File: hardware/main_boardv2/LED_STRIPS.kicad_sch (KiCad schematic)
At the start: 8 parts, among them IC801 SN74LV1T34DBVR, J801 Conn_01x03_Pin

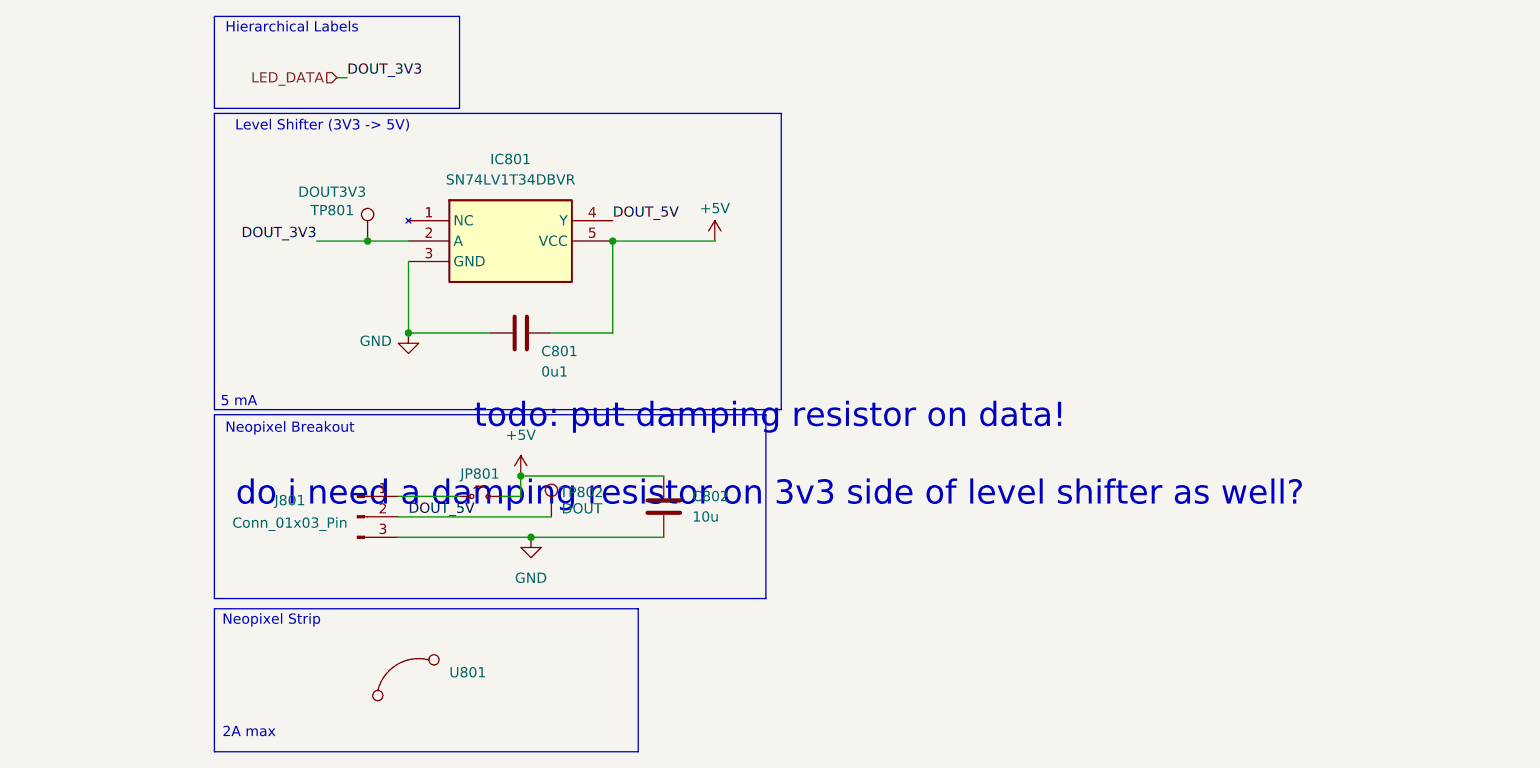
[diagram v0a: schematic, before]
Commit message: dubious hardware schematic 'done'. need to go back and revise passives and verify IC connections, esp the DAC. modified readme
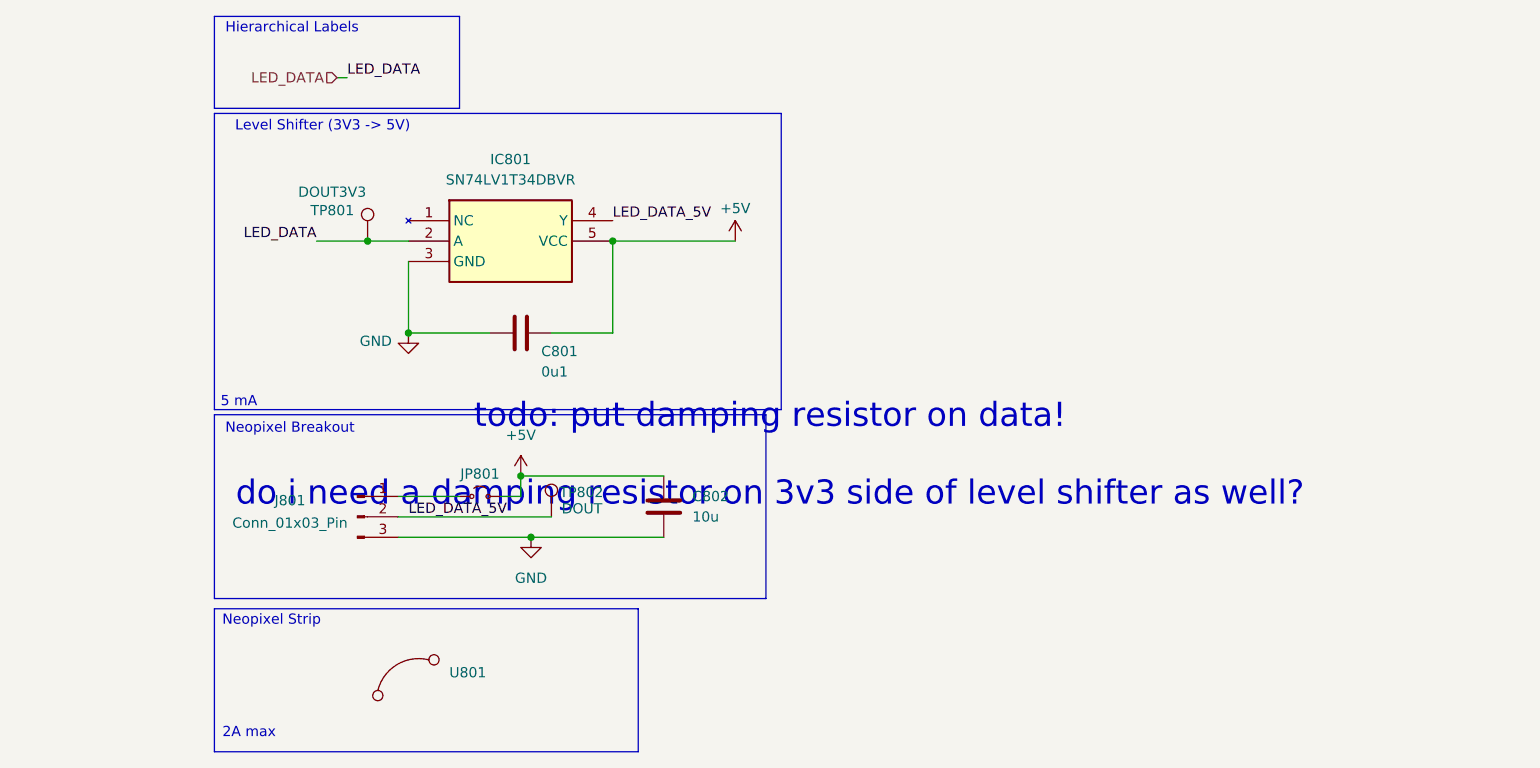
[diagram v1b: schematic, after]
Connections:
- net DOUT_5V renamed LED_DATA_5V
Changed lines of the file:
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@@
 	(wire
 		(pts
-			(xy 63.5 41.91) (xy 76.2 41.91)
+			(xy 63.5 41.91) (xy 78.74 41.91)
 		)
 		(stroke
@@
 		)
 	)
-	(label "DOUT_3V3"
+	(label "LED_DATA_5V"
+		(at 38.1 76.2 0)
+		(effects
+			(font
+				(size 1.27 1.27)
+			)
+			(justify left bottom)
+		)
+	)
+	(label "LED_DATA"
 		(at 30.48 21.59 0)
 		(effects
@@
 		)
 	)
-	(label "DOUT_3V3"
+	(label "LED_DATA"
 		(at 26.67 41.91 180)
 		(effects
@@
 		)
 	)
-	(label "DOUT_5V"
-		(at 38.1 76.2 0)
-		(effects
-			(font
-				(size 1.27 1.27)
-			)
-			(justify left bottom)
-		)
-	)
-	(label "DOUT_5V"
+	(label "LED_DATA_5V"
 		(at 63.5 39.37 0)
 		(effects
@@
 	(symbol
 		(lib_id "power:+5V")
-		(at 76.2 41.91 0)
+		(at 78.74 41.91 0)
 		(unit 1)
 		(exclude_from_sim no)
@@
 		(dnp no)
 		(property "Reference" "#PWR0804"
-			(at 76.2 45.72 0)
+			(at 78.74 45.72 0)
 			(effects
 				(font
@@
 		)
 		(property "Value" "+5V"
-			(at 76.2 37.846 0)
+			(at 78.74 37.846 0)
 			(effects
 				(font
@@
 		)
 		(property "Footprint" ""
-			(at 76.2 41.91 0)
+			(at 78.74 41.91 0)
 			(effects
 				(font
@@
 		)
 		(property "Datasheet" ""
-			(at 76.2 41.91 0)
+			(at 78.74 41.91 0)
 			(effects
 				(font
@@
 		)
 		(property "Description" "Power symbol creates a global label with name \"+5V\""
-			(at 76.2 41.91 0)
-			(effects
-				(font
+			(at 78.74 41.91 0)
+			(effects
+				(font

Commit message: schematic sorta done? resized all RC packages to 0805
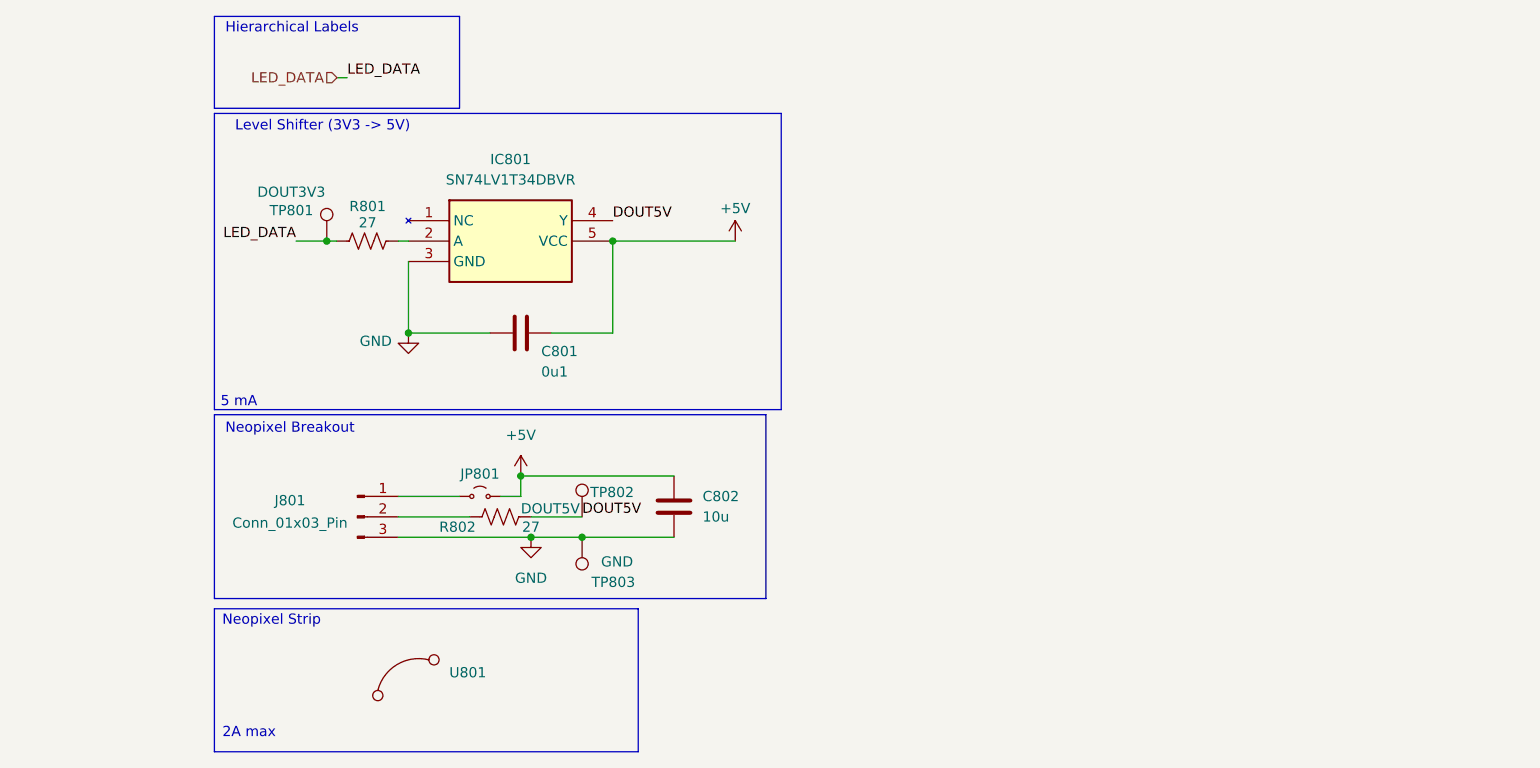
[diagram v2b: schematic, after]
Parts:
- added R801, R802: 27, Resistor_SMD:R_0805_2012Metric, symbol Device:R_US
- added TP803: GND, SamacSys_Parts:bettertestpoint2, symbol Connector:TestPoint
- TP802: value DOUT -> DOUT5V
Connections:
- net GND: now also TP803.1
- net LED_DATA: now also R801.1; no longer IC801.2 (A)
- net LED_DATA_5V renamed DOUT5V
- net DOUT5V: now also R802.2; no longer J801.2 (Pin_2)
- new net: IC801.2 (A), R801.2
- new net: J801.2 (Pin_2), R802.1
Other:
- note removed: "todo: put damping resistor on data! do i need a damping resistor on 3v3 side of level shifter as well?"
- moved on the sheet: C802, TP801, TP802

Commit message: resized all package to 0603
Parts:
- C801: footprint Capacitor_SMD:C_0805_2012Metric -> Capacitor_SMD:C_0603_1608Metric; Mouser Price/Stock https://www.mouser.com/ProductDetail/Walsin/MG21B104K500CT?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 -> (none)
- C802: footprint Capacitor_SMD:C_0805_2012Metric -> Capacitor_SMD:C_0603_1608Metric; Mouser Price/Stock https://www.mouser.com/ProductDetail/Samsung-Electro-Mechan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 -> (none)
- R801, R802: footprint Resistor_SMD:R_0805_2012Metric -> Resistor_SMD:R_0603_1608Metric
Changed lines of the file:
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@@
 			)
 		)
-		(property "Footprint" "Capacitor_SMD:C_0805_2012Metric"
+		(property "Footprint" "Capacitor_SMD:C_0603_1608Metric"
 			(at 72.0852 78.74 0)
 			(effects
@@
 			)
 		)
-		(property "Mouser Price/Stock" "https://www.mouser.com/ProductDetail/Samsung-Electro-Mechanics/CL21A106KPFNNNE?qs=sGAEpiMZZMt7gvpyg0xT8jBAVP%252BdkPhuUJvUBe19zr8%3D"
+		(property "Mouser Price/Stock" ""
 			(at 71.12 74.93 0)
 			(effects
@@
 			)
 		)
-		(property "Footprint" "Resistor_SMD:R_0805_2012Metric"
+		(property "Footprint" "Resistor_SMD:R_0603_1608Metric"
 			(at 33.274 40.894 90)
 			(effects
@@
 			)
 		)
-		(property "Footprint" "Resistor_SMD:R_0805_2012Metric"
+		(property "Footprint" "Resistor_SMD:R_0603_1608Metric"
 			(at 49.784 75.184 90)
 			(effects
@@
 			)
 		)
-		(property "Footprint" "Capacitor_SMD:C_0805_2012Metric"
+		(property "Footprint" "Capacitor_SMD:C_0603_1608Metric"
 			(at 55.88 52.3748 0)
 			(effects
@@
 			)
 		)
-		(property "Mouser Price/Stock" "https://www.mouser.com/ProductDetail/Walsin/MG21B104K500CT?qs=sGAEpiMZZMt7gvpyg0xT8jBHDtGZvLzXjlSfFWC8Jgc2tQbZi0zprA%3D%3D"
+		(property "Mouser Price/Stock" ""
 			(at 52.07 53.34 90)
 			(effects
